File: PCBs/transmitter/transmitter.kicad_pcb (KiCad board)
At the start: 4 copper layers, 34 x 70 mm, 72 parts, among them J1 Conn_01x02, J10 1054550101, J11 LoRa, J2 GPIO, J3 Ethernet, J4 Thermistor (10K), J5 RF24, J6 SWD, J7 I2C, J8 Serial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

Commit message: completed PCB layout
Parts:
- removed H2: MountingHole, MountingHole:MountingHole_2mm
- J4: footprint Connector_PinSocket_2.54mm:PinSocket_1x02_P2.54mm_Vertical -> Connector_PinHeader_2.54mm:PinHeader_1x02_P2.54mm_Vertical
- moved J4 31.0 mm to (141.8, 102.4), turned to -90 degrees
- moved R6 27.5 mm to (145.7, 102.3)
- moved J6 19.2 mm to (160.2, 96.0), turned to 180 degrees
- moved Q1 9.42 mm to (143.1, 123.0), turned to 0 degrees
- moved J2 7.60 mm to (133.9, 87.3), turned to 180 degrees
- moved H3 7.00 mm to (163.1, 79.5)
- moved C8 6.87 mm to (148.5, 92.7), turned to 0 degrees
- moved C9 6.77 mm to (148.5, 94.4), turned to 0 degrees
- moved R14 5.45 mm to (142.8, 107.9)
- moved D3 5.45 mm to (142.7, 106.1)
- moved R15 5.44 mm to (139.0, 107.9)
- moved D4 5.44 mm to (139.0, 106.1), turned to 0 degrees
- moved R10 4.58 mm to (144.4, 118.8)
- moved R11 3.72 mm to (141.1, 111.2)
- moved C12 3.35 mm to (146.3, 117.8)
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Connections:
- U1 pad 10: /CS3 -> /PGOOD
- U1 pad 28: /CHG -> /CS2
- U1 pad 29: /PGOOD -> /CS3
- U1 pad 9: /CS2 -> /CHG
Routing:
- net GND: track 0.00 -> 105.0 mm, vias 0 -> 33
- net /SCL: track 0.00 -> 73.2 mm, vias 0 -> 1
- net /D+: track 0.00 -> 57.7 mm, vias 0 -> 2
- net /SDA: track 0.00 -> 55.7 mm, vias 0 -> 3
- net /MCU/VDIV: track 0.00 -> 51.2 mm, vias 0 -> 2
- net /SCK: track 0.00 -> 47.8 mm, vias 0 -> 4
- net /MOSI: track 0.00 -> 46.8 mm, vias 0 -> 2
- net +3V3: track 0.00 -> 46.1 mm, vias 0 -> 10
- net /D-: track 0.00 -> 43.6 mm, vias 0 -> 2
- net /MISO: track 0.00 -> 41.8 mm, vias 0 -> 2
- net /LEDs/B_a: track 0.00 -> 37.1 mm, vias 0 -> 2
- net /VBAT: track 0.00 -> 34.5 mm
- net /CHG: track 0.00 -> 32.6 mm, vias 0 -> 4
- net VBUS: track 0.00 -> 32.3 mm
- net /PGOOD: track 0.00 -> 32.1 mm, vias 0 -> 4
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- added copper zone on In1.Cu, net +3V3
- added copper zone on In2.Cu, net GND
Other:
- board size 34 x 70 mm -> 34 x 65 mm

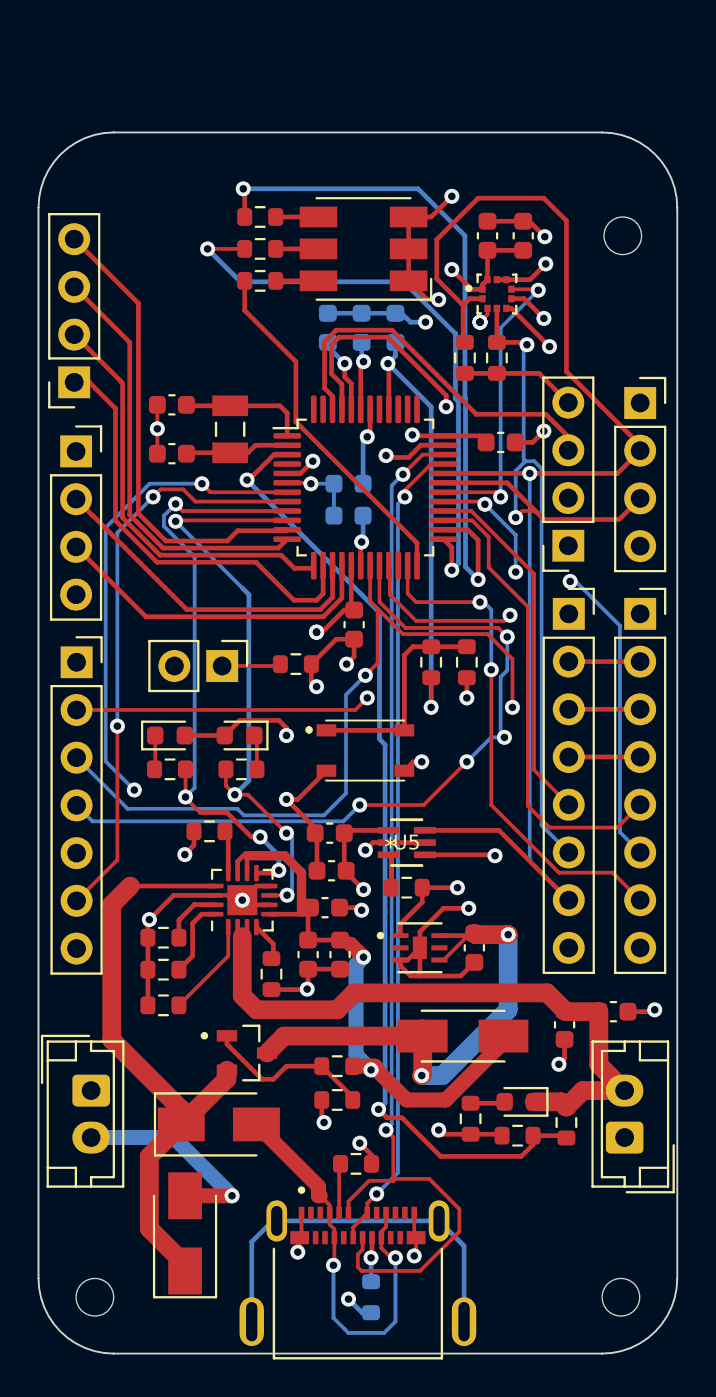
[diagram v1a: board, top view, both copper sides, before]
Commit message: created fabrication outputs
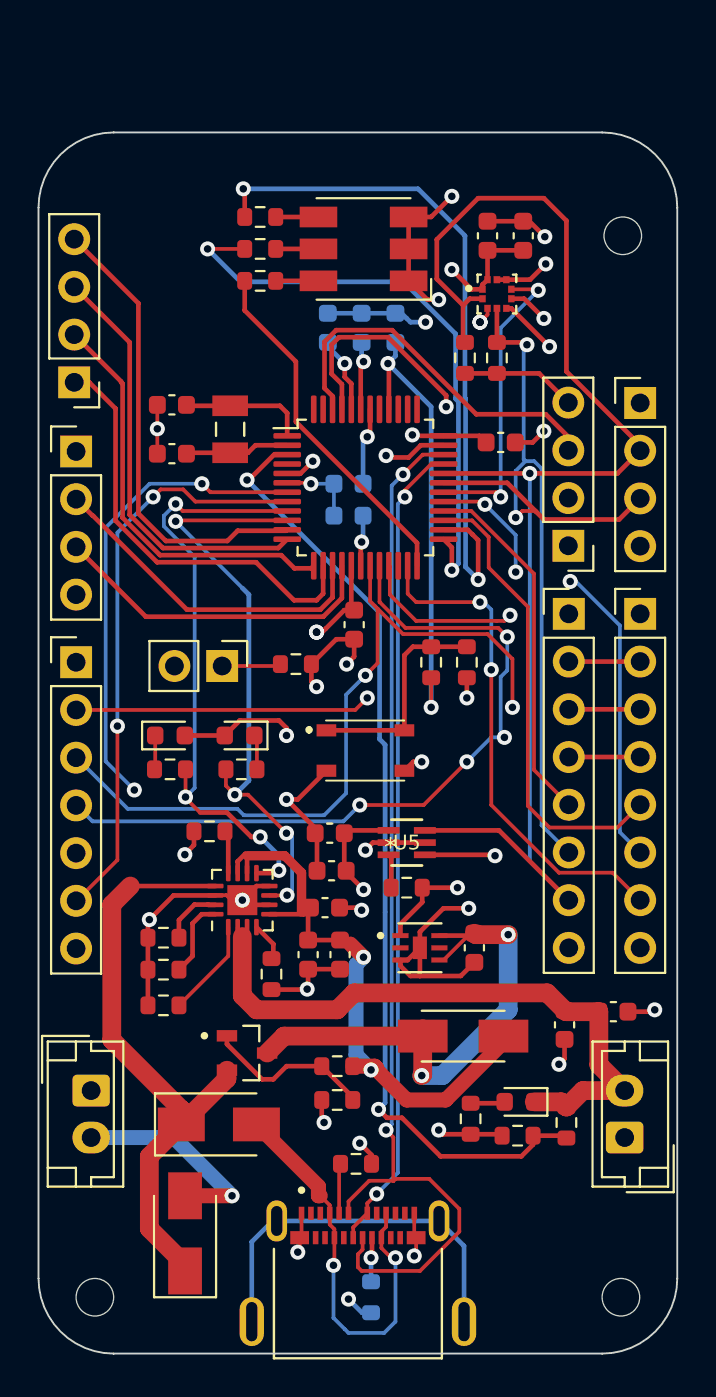
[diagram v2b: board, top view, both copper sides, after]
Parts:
- J11, J3: footprint Connector_PinSocket_2.54mm:PinSocket_1x08_P2.54mm_Vertical -> Connector_PinHeader_2.54mm:PinHeader_1x08_P2.54mm_Vertical
- J2, J6, J7, J8: footprint Connector_PinSocket_2.54mm:PinSocket_1x04_P2.54mm_Vertical -> Connector_PinHeader_2.54mm:PinHeader_1x04_P2.54mm_Vertical
- J5: footprint Connector_PinSocket_2.54mm:PinSocket_1x07_P2.54mm_Vertical -> Connector_PinHeader_2.54mm:PinHeader_1x07_P2.54mm_Vertical

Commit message: created sensor board
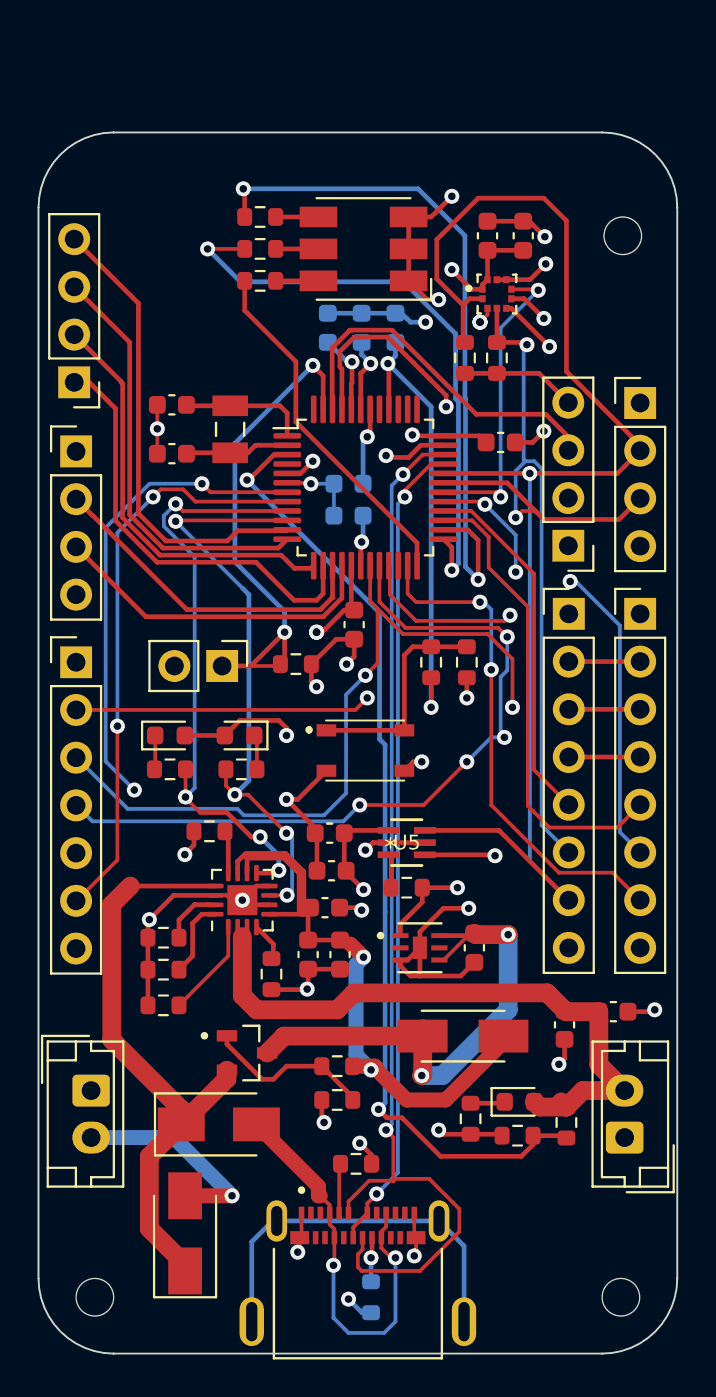
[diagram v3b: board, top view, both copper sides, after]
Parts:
- turned D1 to 0 degrees
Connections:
- D1 pad 1: /VBAT -> Net-(D1-Pad1)
- D1 pad 2: Net-(D1-Pad2) -> /VBAT
- R1 pad 1: Net-(D1-Pad2) -> Net-(D1-Pad1)
- U1 pad 47: unconnected-(U1-Pad47) -> /~{THERM}
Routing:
- net /~{THERM}: track 3.14 -> 28.6 mm, vias 0 -> 2
- net Net-(D1-Pad2): track 1.84 -> 0.00 mm
- net Net-(D1-Pad1): track 0.00 -> 1.84 mm
- net /SWCLK: track 20.9 -> 20.0 mm
- net /SWDIO: track 20.1 -> 19.4 mm
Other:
- board text added: "+"
- board text added: "-"
- board text added: "1"
- board text added: "2"
- board text added: "3"
- board text added: "4"
- board text added: "CL"
- board text added: "CS"
- board text added: "CS1"
- board text added: "CS2"
- board text added: "CS3"
- board text added: "DA"
- board text added: "IRQ"
- board text added: "MI"
- board text added: "MO"
- board text added: "RX"
- board text added: "SCK"
- board text added: "SCL"
- board text added: "SDA"
- board text added: "TX"
